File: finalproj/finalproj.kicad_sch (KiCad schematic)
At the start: 51 parts, among them J10 MotorA Out, J11 MotorB Out, J5 Stepper_Motor_Controller, J7 LIDAR_Connector, J9 RPI_UART_Conn, U1 LM1085-12, U2 LM1085-12, U3 LM1085-5.0, U4 LM1085-3.3, U5 L298N

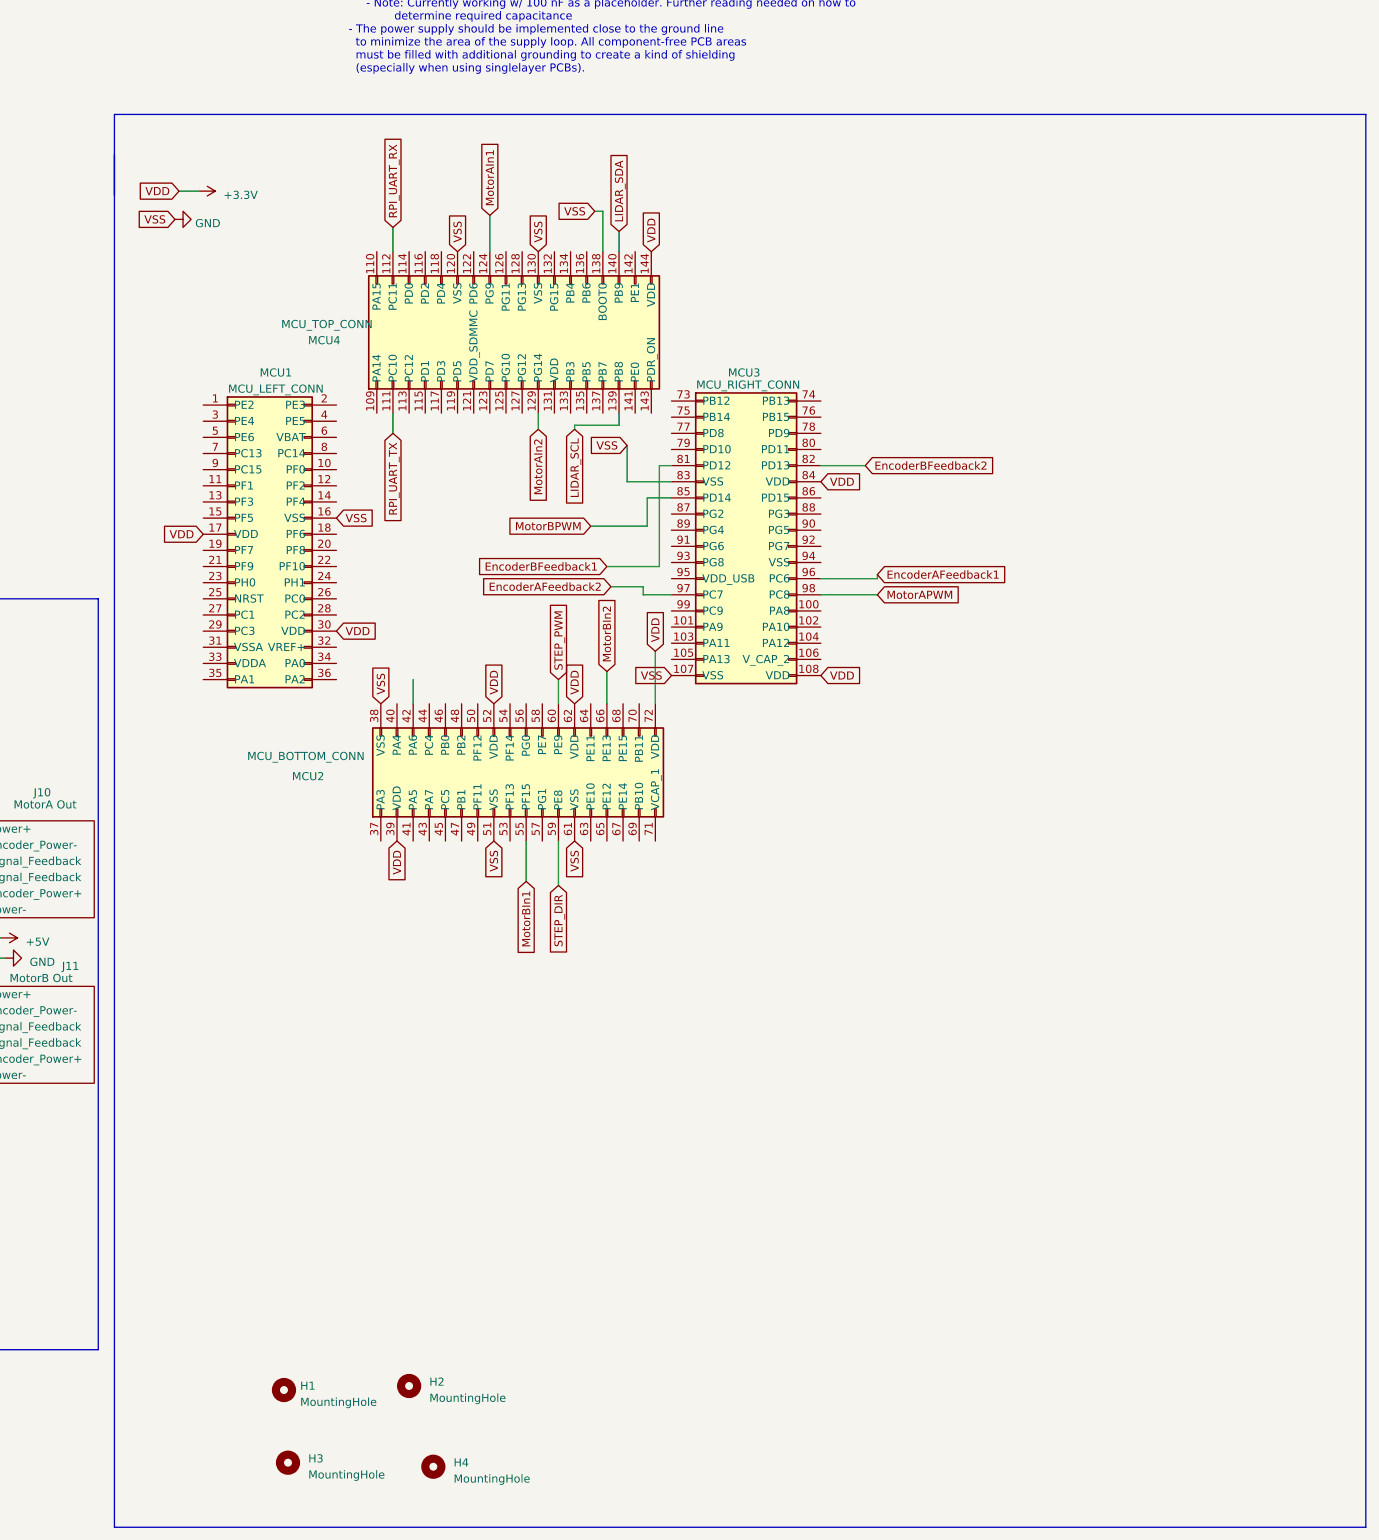
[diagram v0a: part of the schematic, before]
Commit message: Added necessary pin requirements to mainboard
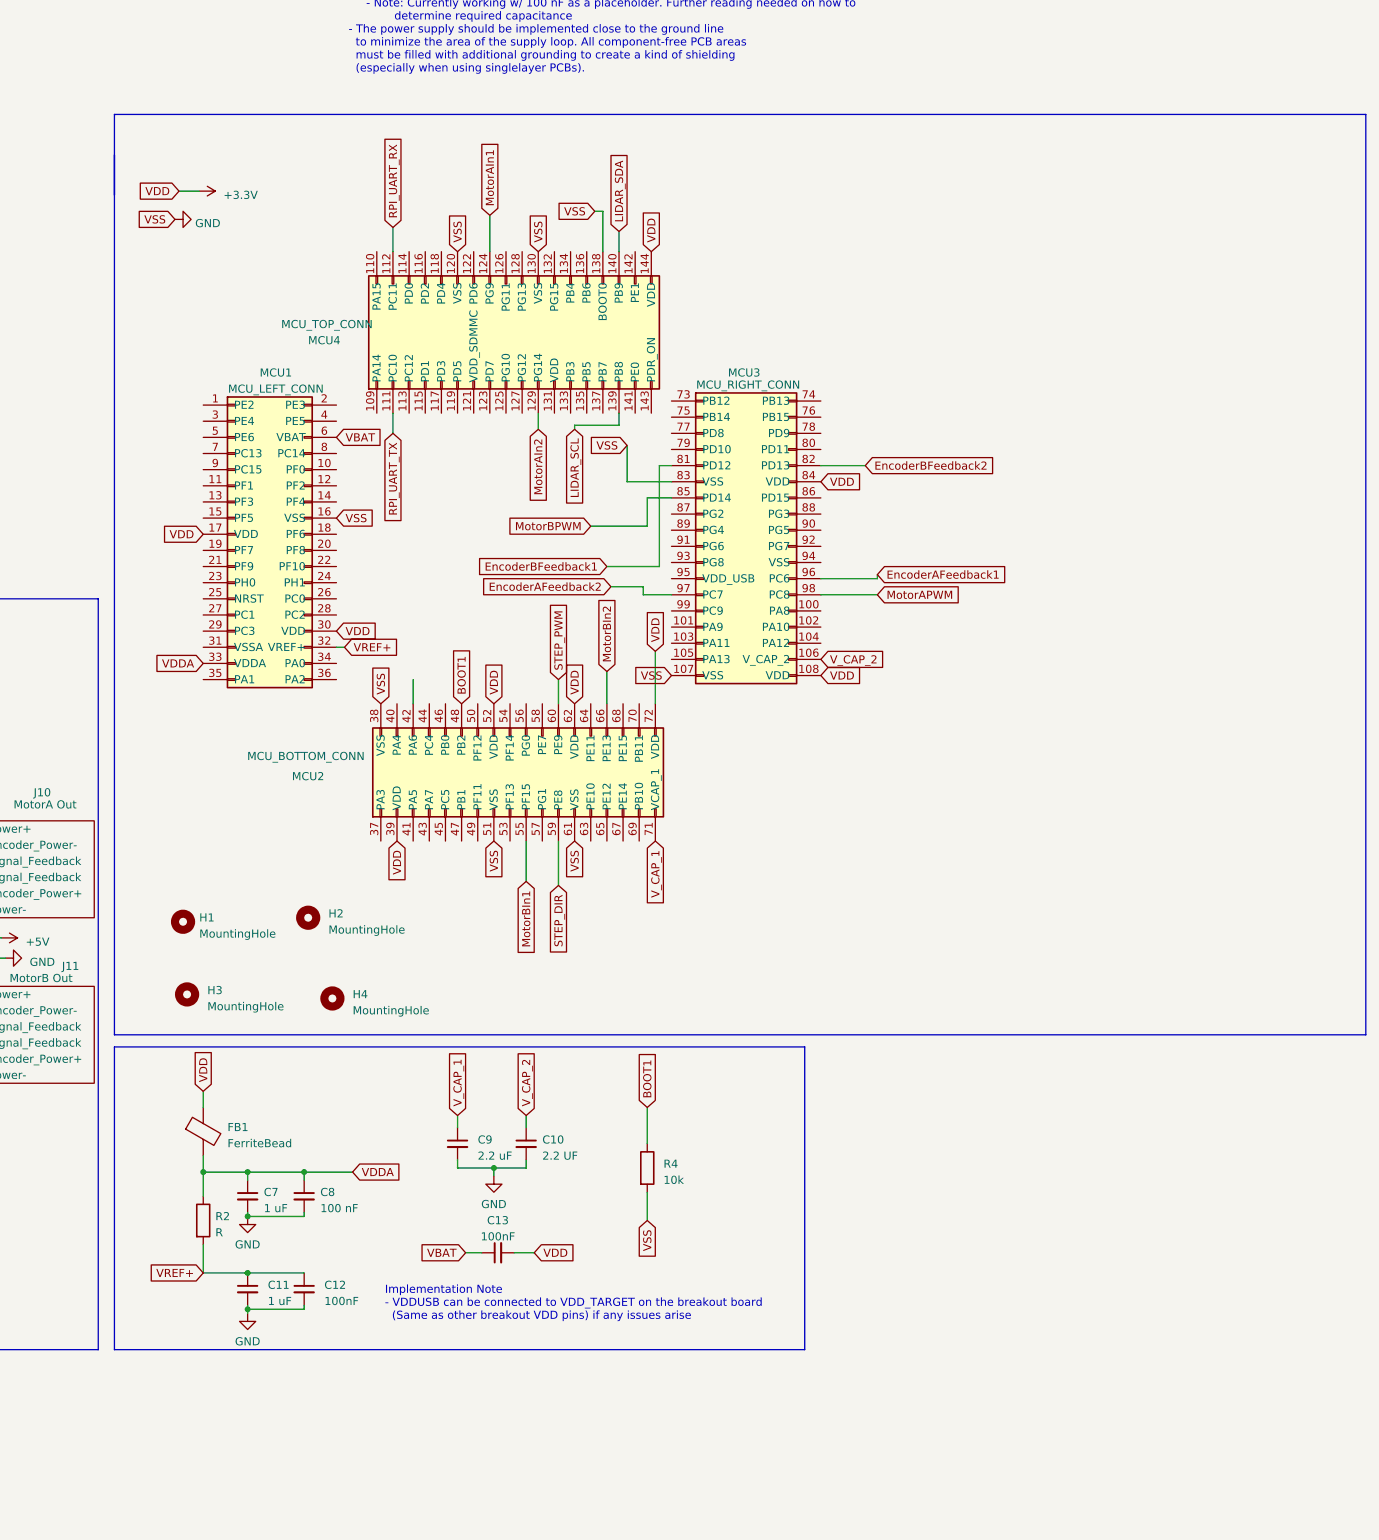
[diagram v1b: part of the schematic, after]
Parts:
- added C10: 2.2 UF, Capacitor_SMD:C_0805_2012Metric, symbol Device:C_Small
- added C11, C7: 1 uF, Capacitor_SMD:C_0805_2012Metric, symbol Device:C_Small
- added C12, C13: 100nF, Capacitor_SMD:C_0805_2012Metric, symbol Device:C_Small
- added C8: 100 nF, Capacitor_SMD:C_0805_2012Metric, symbol Device:C_Small
- added C9: 2.2 uF, Capacitor_SMD:C_0805_2012Metric, symbol Device:C_Small
- added FB1: FerriteBead, symbol Device:FerriteBead
- added R2: R, symbol Device:R
- added R4: 10k, symbol Device:R
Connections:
- net +3.3V: now also C13.2, FB1.1
- net GND: now also C10.2, C11.2, C12.2, C7.2, C8.2, C9.2, R4.2
- net V_CAP_2: now reaches MCU3.106 (V_CAP_2)
- net V_CAP_2: now also C10.1
- net VREF+: now reaches MCU1.32 (VREF+)
- net VREF+: now also C11.1, C12.1, R2.2
- net VDDA: now reaches MCU1.33 (VDDA)
- net VDDA: now also C7.1, C8.1, FB1.2, R2.1
- net VBAT: now reaches MCU1.6 (VBAT)
- net VBAT: now also C13.1
- net BOOT1: now reaches MCU2.48 (PB2)
- net BOOT1: now also R4.1
- net V_CAP_1: now reaches MCU2.71 (VCAP_1)
- net V_CAP_1: now also C9.1
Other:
- note added: "Implementation Note - VDDUSB can be connected to VDD_TARGET on the breakout board (Same as other breakout VDD pins) if any issues arise"
- moved on the sheet: H1, H2, H3, H4

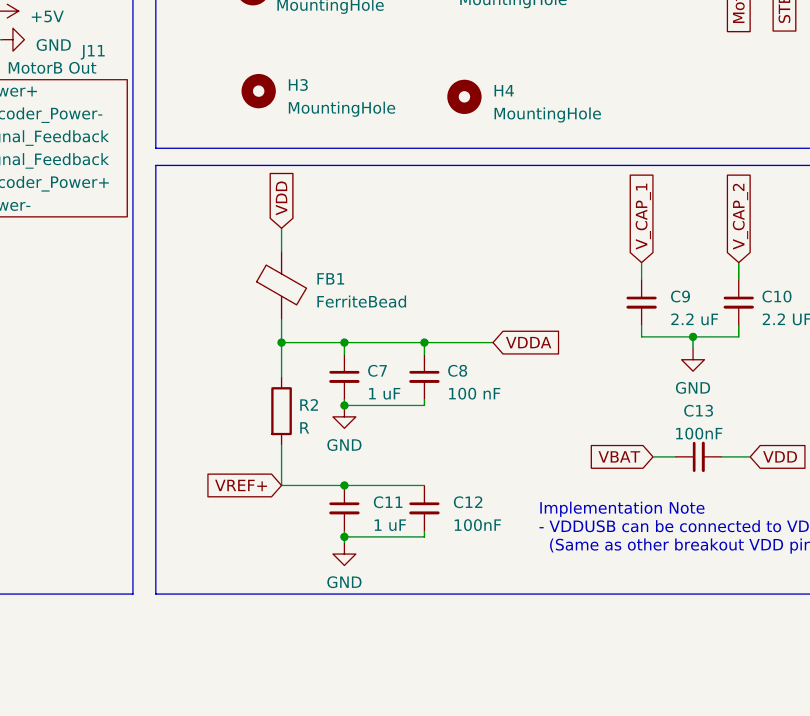
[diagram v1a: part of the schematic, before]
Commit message: Added recommended decoupling components to main board - removed parts deemed unnecessary or ambiguous
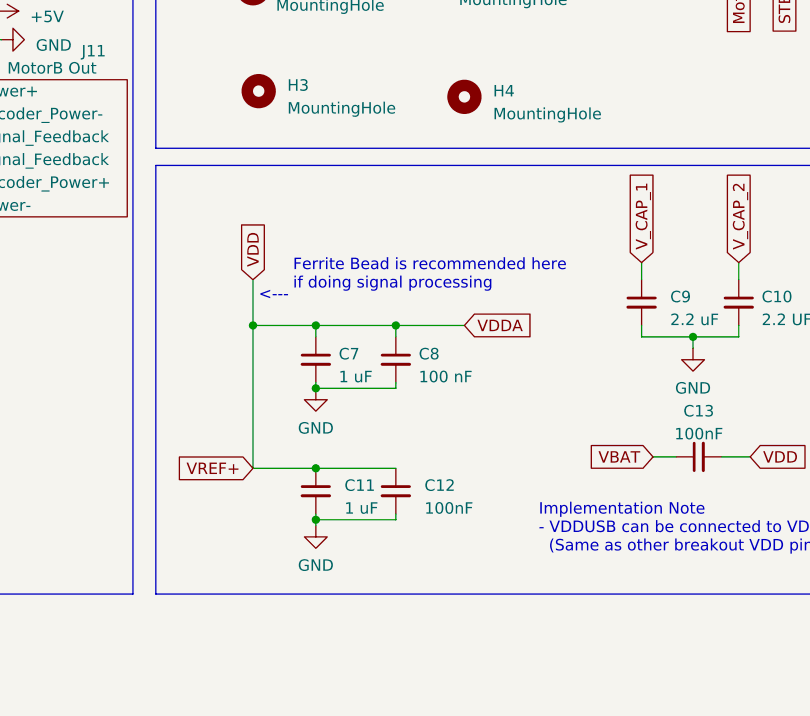
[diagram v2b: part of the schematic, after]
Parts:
- removed FB1: FerriteBead, symbol Device:FerriteBead
- removed R2: R, symbol Device:R
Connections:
- net VDDA is gone; now on net +3.3V: C7.1, C8.1, MCU1.33 (VDDA)
- net VREF+ is gone; now on net +3.3V: C11.1, C12.1, MCU1.32 (VREF+)
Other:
- note added: "<---"
- note added: "Ferrite Bead is recommended here if doing signal processing"
- moved on the sheet: C11, C12, C7, C8

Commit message: Mainboard updated to SMT32F401 standards
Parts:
- removed R4: 10k, symbol Device:R
- added C14, C15, C16, C17, C18, C19, C22: 100 nF, symbol Device:C_Small
- added C20: 4.7 uF, symbol Device:C_Small
- added C21, C36, C37: 4.7uF, symbol Device:C_Small
- added C23: 1uF, symbol Device:C_Small
- added C38: 0.1uF, symbol Device:C_Small
- added C39: 100nF, Capacitor_SMD:C_0805_2012Metric, symbol Device:C_Small
- added J1, J2, J3: Conn_01x01, symbol Connector_Generic:Conn_01x01
- added J4: Programmer_Conn, symbol Connector_Generic:Conn_01x06
- added R2: 10k, symbol Device:R_Small
- added SW1, SW2: SW_DPDT_x2, symbol Switch:SW_DPDT_x2
- added SW3: SW_Push, symbol Switch:SW_Push
- added U6: STM32F401RBTx, Package_QFP:LQFP-64_10x10mm_P0.5mm, symbol MCU_ST_STM32F4:STM32F401RBTx
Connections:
- net +12V: now also J1.1 (Pin_1)
- net +3.3V: now also C14.2, C15.2, C16.2, C17.2, C18.2, C19.2, C20.2, C22.2, C23.2, C39.2, J3.1 (Pin_1), J4.1 (Pin_1), SW1.1 (A), SW2.1 (A), U6.19 (VDD), U6.32 (VDD), U6.48 (VDD), U6.64 (VDD)
- net +5V: now also J2.1 (Pin_1)
- net EncoderAFeedback1: now also U6.37 (PC6)
- net EncoderAFeedback2: now also U6.38 (PC7)
- net GND: now also C14.1, C15.1, C16.1, C17.1, C18.1, C19.1, C20.1, C21.1, C22.1, C23.1, C36.1, C37.1, C38.2, J4.3 (Pin_3), SW1.3 (C), SW2.3 (C), SW3.2, U6.12 (VSSA), U6.18 (VSS), U6.31 (VSS), U6.47 (VSS), U6.63 (VSS)
- net LIDAR_SCL: now also U6.61 (PB8)
- net LIDAR_SDA: now also U6.62 (PB9)
- net MotorAIn2: now also U6.3 (PC14)
- net MotorAPWM: now also U6.39 (PC8)
- net RPI_UART_RX: now also U6.52 (PC11)
- net RPI_UART_TX: now also U6.51 (PC10)
- new net: C39.1, U6.1 (VBAT)
- new net: C36.2, C37.2, U6.13 (VREF+)
- new net: SW1.2 (B), U6.28 (PB2)
- new net: R2.1, SW2.2 (B)
- new net: C21.2, U6.30 (VCAP1)
- new net: R2.2, U6.60 (BOOT0)
- new net NRST: C38.1, J4.5 (Pin_5), SW3.1, U6.7 (NRST)
- new net SWCLK: J4.2 (Pin_2), U6.50 (PA15)
- new net SWDIO: J4.4 (Pin_4), U6.46 (PA13)
- new net SWO: J4.6 (Pin_6)
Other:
- note added: "BOOT1"
- note added: "External Power Supply GPIO Pins"
- note added: "Labels Requiring Substitutions: - Connect PG3 equivalent to SWO - Connect PG9 equivalent to MotorAln1"
- note added: "MCU"
- note added: "VDD-VSS Decoupling"
- note added: "VDDA-VSSA Decoupling"
- moved on the sheet: C10, C11, C12, C13, C29, C30, C31, C32, C33, C34, C5, C6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

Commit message: Assigned footprints, reassigned tags
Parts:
- removed C10: 2.2 UF, Capacitor_SMD:C_0805_2012Metric, symbol Device:C_Small
- removed C11, C7: 1 uF, Capacitor_SMD:C_0805_2012Metric, symbol Device:C_Small
- removed C12, C13: 100nF, Capacitor_SMD:C_0805_2012Metric, symbol Device:C_Small
- removed C8: 100 nF, Capacitor_SMD:C_0805_2012Metric, symbol Device:C_Small
- removed C9: 2.2 uF, Capacitor_SMD:C_0805_2012Metric, symbol Device:C_Small
- removed MCU1: MCU_LEFT_CONN, MCU_SOCKETS:MCU1_SOCKET, symbol Connector_Generic:Conn_02x18_Odd_Even
- removed MCU2: MCU_BOTTOM_CONN, MCU_SOCKETS:MCU2_SOCKETS, symbol Connector_Generic:Conn_02x18_Odd_Even
- removed MCU3: MCU_RIGHT_CONN, MCU_SOCKETS:MCU3_SOCKETS, symbol Connector_Generic:Conn_02x18_Odd_Even
- removed MCU4: MCU_TOP_CONN, MCU_SOCKETS:MCU4_SOCKETS, symbol Connector_Generic:Conn_02x18_Odd_Even
- removed U6: STM32F401RBTx, Package_QFP:LQFP-64_10x10mm_P0.5mm, symbol MCU_ST_STM32F4:STM32F401RBTx
- added C40, C41, C42, C43: 20pF, Capacitor_SMD:C_0805_2012Metric, symbol Device:C_Small
- added J6: Conn_01x01, Connector_PinHeader_2.54mm:PinHeader_1x01_P2.54mm_Vertical, symbol Connector_Generic:Conn_01x01
- added R10, R8, R9: 0, Resistor_SMD:R_1206_3216Metric_Pad1.30x1.75mm_HandSolder, symbol Device:R_Small
- added R4: 10k, Resistor_SMD:R_1206_3216Metric_Pad1.30x1.75mm_HandSolder, symbol Device:R_Small
- added R6: 0, Connector_PinHeader_2.54mm:PinHeader_1x06_P2.54mm_Vertical, symbol Device:R_Small
- added U7: STM32F401RCTx, Package_QFP:LQFP-64_10x10mm_P0.5mm, symbol MCU_ST_STM32F4:STM32F401RCTx
- added Y1: 25 MHz, ABLS-25.000MHZ-B2F-T:XTAL_ABLS-25.000MHZ-B2F-T, symbol Device:Crystal
- added Y2: 32.768 KHz, Crystal:Crystal_SMD_3215-2Pin_3.2x1.5mm, symbol Device:Crystal
- C14, C15, C16, C17, C18, C19, C20, C21, C22, C23, C36, C37, C38: footprint (none) -> Capacitor_SMD:C_0805_2012Metric
- J1, J2, J3: footprint (none) -> Connector_PinHeader_2.54mm:PinHeader_1x01_P2.54mm_Vertical
- J4: footprint (none) -> Connector_PinHeader_2.54mm:PinHeader_1x06_P2.54mm_Vertical
- R2: footprint (none) -> Resistor_SMD:R_1206_3216Metric_Pad1.30x1.75mm_HandSolder
- SW1, SW2: footprint (none) -> EG-1206A:SLIDE-SWITCH
- SW3: footprint (none) -> Button_Switch_THT:SW_PUSH_6mm
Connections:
- net +3.3V: now also U7.19 (VDD), U7.32 (VDD), U7.48 (VDD), U7.64 (VDD)
- net EncoderAFeedback1: now also U7.41 (PA8)
- net EncoderAFeedback2: now also U7.42 (PA9)
- net EncoderBFeedback1: now also U7.14 (PA0)
- net EncoderBFeedback2: now also U7.15 (PA1)
- net GND: now also C40.1, C41.1, C42.1, C43.1, J6.1 (Pin_1), U7.12 (VSSA), U7.18 (VSS), U7.31 (VSS), U7.47 (VSS), U7.63 (VSS)
- net LIDAR_SCL: now also U7.61 (PB8)
- net LIDAR_SDA: now also U7.62 (PB9)
- net MotorAIn1: now also U7.37 (PC6)
- net MotorAIn2: now also U7.38 (PC7)
- net MotorAPWM: now also U7.43 (PA10)
- net MotorBIn1: now also U7.39 (PC8)
- net MotorBIn2: now also U7.40 (PC9)
- net MotorBPWM: now also U7.16 (PA2)
- net NRST: now also U7.7 (NRST)
- net RPI_UART_RX: now also U7.59 (PB7)
- net RPI_UART_TX: now also U7.58 (PB6)
- net STEP_DIR: now also U7.36 (PB15)
- net STEP_PWM: now also U7.22 (PA6)
- net SWCLK: now also U7.49 (PA14)
- net SWDIO: now also U7.46 (PA13)
- net SWO: now also U7.55 (PB3)
- net at C39.1: now also U7.1 (VBAT)
- net at C36.2, C37.2: now also U7.13 (VREF+)
- net at SW1.2 (B): now also R4.2
- net at C21.2: now also U7.30 (VCAP1)
- net at R2.2: now also U7.60 (BOOT0)
- new net: R4.1, U7.28 (PB2)
- new net: C40.2, R6.1, Y1.2
- new net: R6.2, U7.3 (PC14)
- new net: R8.1, U7.4 (PC15)
- new net: C41.2, R8.2, Y1.1
- new net: C43.2, R9.2, Y2.1
- new net: C42.2, R10.1, Y2.2
- new net: R9.1, U7.6 (PH1)
- new net: R10.2, U7.5 (PH0)
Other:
- note added: "OSC_IN"
- note added: "OSC_OUT"
- note removed: "<---"
- note removed: "Ferrite Bead is recommended here if doing signal processing"
- note removed: "Implementation Note - VDDUSB can be connected to VDD_TARGET on the breakout board (Same as other breakout VDD pins) if any issues arise"
- note removed: "Labels Requiring Substitutions: - Connect PG3 equivalent to SWO - Connect PG9 equivalent to MotorAln1"
- moved on the sheet: C14, C15, C16, C17, C18, C19, C20, C22, C23, J1, J2, J3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

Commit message: finished pcb2 placement
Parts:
- R6: footprint Connector_PinHeader_2.54mm:PinHeader_1x06_P2.54mm_Vertical -> Resistor_SMD:R_1206_3216Metric_Pad1.30x1.75mm_HandSolder
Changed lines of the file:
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@@
       (effects (font (size 1.27 1.27)))
     )
-    (property "Footprint" "Connector_PinHeader_2.54mm:PinHeader_1x06_P2.54mm_Vertical" (at 244.348 97.79 0)
+    (property "Footprint" "Resistor_SMD:R_1206_3216Metric_Pad1.30x1.75mm_HandSolder" (at 244.348 97.79 0)
       (effects (font (size 1.27 1.27)) hide)
     )
